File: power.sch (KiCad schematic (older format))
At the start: 28 parts, among them U701 TPS61022, U702 TLV62585

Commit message: Continue part picking
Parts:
- D701: value BAT42 -> BAS16; footprint Diode_SMD:D_SOD-123 -> Diode_SMD:D_SOT-23_ANK; Current (none) -> 150mA; Digikey BAT42W-E3-08CT-ND -> BAS16-FDICT-ND; LCSC (none) -> C69162*; MPN BAT42W-E3-08 -> BAS16-7-F; Note DIODE SCHOTTKY 30V 200MA SOD123 -> DIODE GEN PURP 75V 200MA SOT23-3
- gave numbers to parts that had none: 8
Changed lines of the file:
@@
 P 2950 1000
 F 0 "D701" H 2950 784 50  0000 C CNN
-F 1 "BAT42" H 2950 875 50  0000 C CNN
-F 2 "Diode_SMD:D_SOD-123" H 2950 1000 50  0001 C CNN
+F 1 "BAS16" H 2950 875 50  0000 C CNN
+F 2 "Diode_SMD:D_SOT-23_ANK" H 2950 1000 50  0001 C CNN
 F 3 "~" H 2950 1000 50  0001 C CNN
-F 4 "BAT42W-E3-08" H 2950 1000 50  0001 C CNN "MPN"
-F 5 "BAT42W-E3-08CT-ND" H 2950 1000 50  0001 C CNN "Digikey"
-F 6 "DIODE SCHOTTKY 30V 200MA SOD123" H 2950 1000 50  0001 C CNN "Note"
+F 4 "BAS16-7-F" H 2950 1000 50  0001 C CNN "MPN"
+F 5 "BAS16-FDICT-ND" H 2950 1000 50  0001 C CNN "Digikey"
+F 6 "DIODE GEN PURP 75V 200MA SOT23-3" H 2950 1000 50  0001 C CNN "Note"
+F 7 "150mA" H 2950 1000 50  0001 C CNN "Current"
+F 8 "C69162*" H 2950 1000 50  0001 C CNN "LCSC"
 	1    2950 1000
 	-1   0    0    1
@@
 AR Path="/5FAC6B33/5FBB8CF8" Ref="R?"  Part="1"
 AR Path="/5FCEDB09/5FAC6B33/5FBB8CF8" Ref="R?"  Part="1"
-AR Path="/5FAF778C/5FBB8CF8" Ref="R?"  Part="1"
-F 0 "R?" V 3450 3750 50  0000 C CNN
+AR Path="/5FAF778C/5FBB8CF8" Ref="R804"  Part="1"
+F 0 "R804" V 3450 3750 50  0000 C CNN
 F 1 "59k" V 3350 3750 50  0000 C CNN
 F 2 "Resistor_SMD:R_0603_1608Metric" H 3600 3750 50  0001 C CNN
@@
 $EndComp
 $Comp
-L power:+BATT #PWR?
+L power:+BATT #PWR0198
 U 1 1 5FE17E12
 P 950 1700
-F 0 "#PWR?" H 950 1550 50  0001 C CNN
+F 0 "#PWR0198" H 950 1550 50  0001 C CNN
 F 1 "+BATT" H 965 1873 50  0000 C CNN
 F 2 "" H 950 1700 50  0001 C CNN
@@
 	1250 3650 1600 3650
 $Comp
-L Device:Q_PMOS_GSD Q?
+L Device:Q_PMOS_GSD Q801
 U 1 1 5FAACE37
 P 5550 1950
-AR Path="/5FAF778C/5FAACE37" Ref="Q?"  Part="1"
+AR Path="/5FAF778C/5FAACE37" Ref="Q801"  Part="1"
 AR Path="/5FCEDB09/5FAC6B33/5FAACE37" Ref="Q?"  Part="1"
-F 0 "Q?" V 5892 1950 50  0000 C CNN
+F 0 "Q801" V 5892 1950 50  0000 C CNN
 F 1 "DMMT5401" V 5801 1950 50  0000 C CNN
 F 2 "Package_TO_SOT_SMD:SOT-23-6" H 5750 2050 50  0001 C CNN
@@
 $EndComp
 $Comp
-L Device:Q_DUAL_PNP_PNP_C1B1B2C2E2E1 Q?
+L Device:Q_DUAL_PNP_PNP_C1B1B2C2E2E1 Q802
 U 1 1 5FAACE41
 P 5200 2200
-AR Path="/5FAF778C/5FAACE41" Ref="Q?"  Part="1"
+AR Path="/5FAF778C/5FAACE41" Ref="Q802"  Part="1"
 AR Path="/5FCEDB09/5FAC6B33/5FAACE41" Ref="Q?"  Part="1"
-F 0 "Q?" H 5391 2200 50  0000 L CNN
+F 0 "Q802" H 5391 2200 50  0000 L CNN
 F 1 "DMMT5401" H 5391 2245 50  0001 L CNN
 F 2 "Package_TO_SOT_SMD:SOT-23-6" H 5400 2300 50  0001 C CNN
@@
 P 5100 2650
 AR Path="/5FAACE54" Ref="R?"  Part="1"
-AR Path="/5FAF778C/5FAACE54" Ref="R?"  Part="1"
+AR Path="/5FAF778C/5FAACE54" Ref="R802"  Part="1"
 AR Path="/5FCEDB09/5FAC6B33/5FAACE54" Ref="R?"  Part="1"
-F 0 "R?" H 5168 2696 50  0000 L CNN
+F 0 "R802" H 5168 2696 50  0000 L CNN
 F 1 "10k" H 5168 2605 50  0000 L CNN
 F 2 "Resistor_SMD:R_0603_1608Metric" H 5100 2650 60  0001 C CNN
@@
 P 6000 2650
 AR Path="/5FED2126/5FAACE5A" Ref="R?"  Part="1"
-AR Path="/5FAF778C/5FAACE5A" Ref="R?"  Part="1"
+AR Path="/5FAF778C/5FAACE5A" Ref="R803"  Part="1"
 AR Path="/5FCEDB09/5FAC6B33/5FAACE5A" Ref="R?"  Part="1"
-F 0 "R?" H 5932 2604 50  0000 R CNN
+F 0 "R803" H 5932 2604 50  0000 R CNN
 F 1 "47.5k" H 5932 2695 50  0000 R CNN
 F 2 "Resistor_SMD:R_0603_1608Metric" H 6000 2650 60  0001 C CNN
@@
 	6000 2500 6000 2450
 $Comp
-L power:GND #PWR?
+L power:GND #PWR0199
 U 1 1 5FAACE63
 P 6000 2850
-AR Path="/5FAF778C/5FAACE63" Ref="#PWR?"  Part="1"
+AR Path="/5FAF778C/5FAACE63" Ref="#PWR0199"  Part="1"
 AR Path="/5FCEDB09/5FAC6B33/5FAACE63" Ref="#PWR?"  Part="1"
-F 0 "#PWR?" H 6000 2600 50  0001 C CNN
+F 0 "#PWR0199" H 6000 2600 50  0001 C CNN
 F 1 "GND" H 6005 2677 50  0000 C CNN
 F 2 "" H 6000 2850 50  0001 C CNN
@@
 	6000 2850 6000 2800
 $Comp
-L power:GND #PWR?
+L power:GND #PWR0200
 U 1 1 5FAACE6A
 P 5100 2850
-AR Path="/5FAF778C/5FAACE6A" Ref="#PWR?"  Part="1"
+AR Path="/5FAF778C/5FAACE6A" Ref="#PWR0200"  Part="1"
 AR Path="/5FCEDB09/5FAC6B33/5FAACE6A" Ref="#PWR?"  Part="1"
-F 0 "#PWR?" H 5100 2600 50  0001 C CNN
+F 0 "#PWR0200" H 5100 2600 50  0001 C CNN
 F 1 "GND" H 5105 2677 50  0000 C CNN
 F 2 "" H 5100 2850 50  0001 C CNN
@@
 	5550 2150 5550 2450
 $Comp
-L Device:Q_DUAL_PNP_PNP_C1B1B2C2E2E1 Q?
+L Device:Q_DUAL_PNP_PNP_C1B1B2C2E2E1 Q803
 U 1 1 5FAACE79
 P 5900 2200
-AR Path="/5FAF778C/5FAACE79" Ref="Q?"  Part="1"
+AR Path="/5FAF778C/5FAACE79" Ref="Q803"  Part="1"
 AR Path="/5FCEDB09/5FAC6B33/5FAACE79" Ref="Q?"  Part="2"
-F 0 "Q?" H 6091 2154 50  0000 L CNN
+F 0 "Q803" H 6091 2154 50  0000 L CNN
 F 1 "DMMT5401" H 6091 2245 50  0000 L CNN
 F 2 "Package_TO_SOT_SMD:SOT-23-6" H 6100 2300 50  0001 C CNN
@@
 AR Path="/5E5C8043/5FC95C56" Ref="R?"  Part="1"
 AR Path="/5E715318/5FC95C56" Ref="R?"  Part="1"
-AR Path="/5FAF778C/5FC95C56" Ref="R?"  Part="1"
-F 0 "R?" H 1982 1904 50  0000 R CNN
+AR Path="/5FAF778C/5FC95C56" Ref="R801"  Part="1"
+F 0 "R801" H 1982 1904 50  0000 R CNN
 F 1 "100k" H 1982 1995 50  0000 R CNN
 F 2 "Resistor_SMD:R_0603_1608Metric" V 2090 1940 50  0001 C CNN
@@
 	2550 2050 2600 2050
 $Comp
-L power:+BATT #PWR?
+L power:+BATT #PWR0201
 U 1 1 5FCEFB73
 P 1200 5400
-F 0 "#PWR?" H 1200 5250 50  0001 C CNN
+F 0 "#PWR0201" H 1200 5250 50  0001 C CNN
 F 1 "+BATT" H 1215 5573 50  0000 C CNN
 F 2 "" H 1200 5400 50  0001 C CNN
@@
 $EndComp
 $Comp
-L Connector_Generic:Conn_01x02 J?
+L Connector_Generic:Conn_01x02 J801
 U 1 1 5FCF08CD
 P 1450 5500
-F 0 "J?" H 1530 5492 50  0000 L CNN
+F 0 "J801" H 1530 5492 50  0000 L CNN
 F 1 "Conn_01x02" H 1530 5401 50  0000 L CNN
 F 2 "Connector_PinHeader_2.54mm:PinHeader_1x02_P2.54mm_Vertical" H 1450 5500 50  0001 C CNN
@@
 	1200 5600 1200 5700
 $Comp
-L power:GND #PWR?
+L power:GND #PWR0202
 U 1 1 5FCF766A
 P 1200 5700
-AR Path="/5FAF778C/5FCF766A" Ref="#PWR?"  Part="1"
+AR Path="/5FAF778C/5FCF766A" Ref="#PWR0202"  Part="1"
 AR Path="/5FCEDB09/5FAC6B33/5FCF766A" Ref="#PWR?"  Part="1"
-F 0 "#PWR?" H 1200 5450 50  0001 C CNN
+F 0 "#PWR0202" H 1200 5450 50  0001 C CNN
 F 1 "GND" H 1205 5527 50  0000 C CNN
 F 2 "" H 1200 5700 50  0001 C CNN

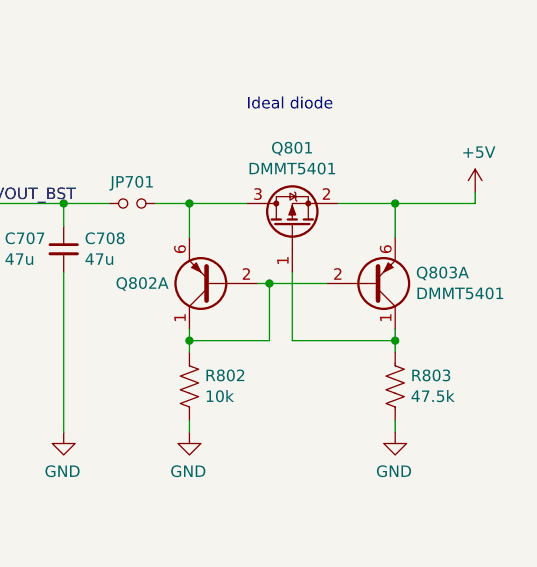
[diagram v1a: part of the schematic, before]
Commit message: Modified layout for Smoke, Fixed Ideal Diode
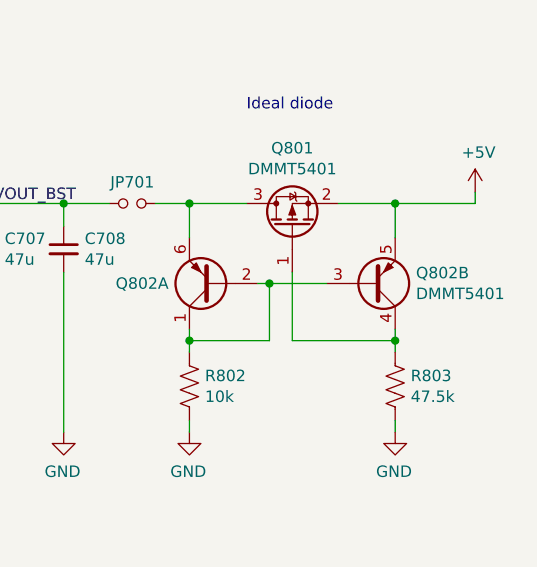
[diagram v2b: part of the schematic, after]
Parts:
- renumbered Q803 to Q802
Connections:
- net +5V: now also Q802.5 (E2); no longer Q802.6 (E1)
- net at Q801.1 (G), R803.2: now also Q802.4 (C2); no longer Q802.1 (C1)
- net at Q802.1 (C1), Q802.2 (B1), R802.1: now also Q802.3 (B2); no longer Q802.2 (B1)
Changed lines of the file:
@@
 	5550 2150 5550 2450
 $Comp
-L Device:Q_DUAL_PNP_PNP_C1B1B2C2E2E1 Q803
-U 1 1 5FAACE79
+L Device:Q_DUAL_PNP_PNP_C1B1B2C2E2E1 Q802
+U 2 1 5FAACE79
 P 5900 2200
-AR Path="/5FAF778C/5FAACE79" Ref="Q803"  Part="1"
+AR Path="/5FAF778C/5FAACE79" Ref="Q802"  Part="2"
 AR Path="/5FCEDB09/5FAC6B33/5FAACE79" Ref="Q?"  Part="2"
-F 0 "Q803" H 6091 2154 50  0000 L CNN
+F 0 "Q802" H 6091 2154 50  0000 L CNN
 F 1 "DMMT5401" H 6091 2245 50  0000 L CNN
 F 2 "Package_TO_SOT_SMD:SOT-23-6" H 6100 2300 50  0001 C CNN
@@
 F 6 "TRANS 2PNP 150V 0.2A SOT26" H 5900 2200 50  0001 C CNN "Note"
 F 7 "C154733" H 5900 2200 50  0001 C CNN "LCSC"
-	1    5900 2200
+	2    5900 2200
 	1    0    0    1
 $EndComp

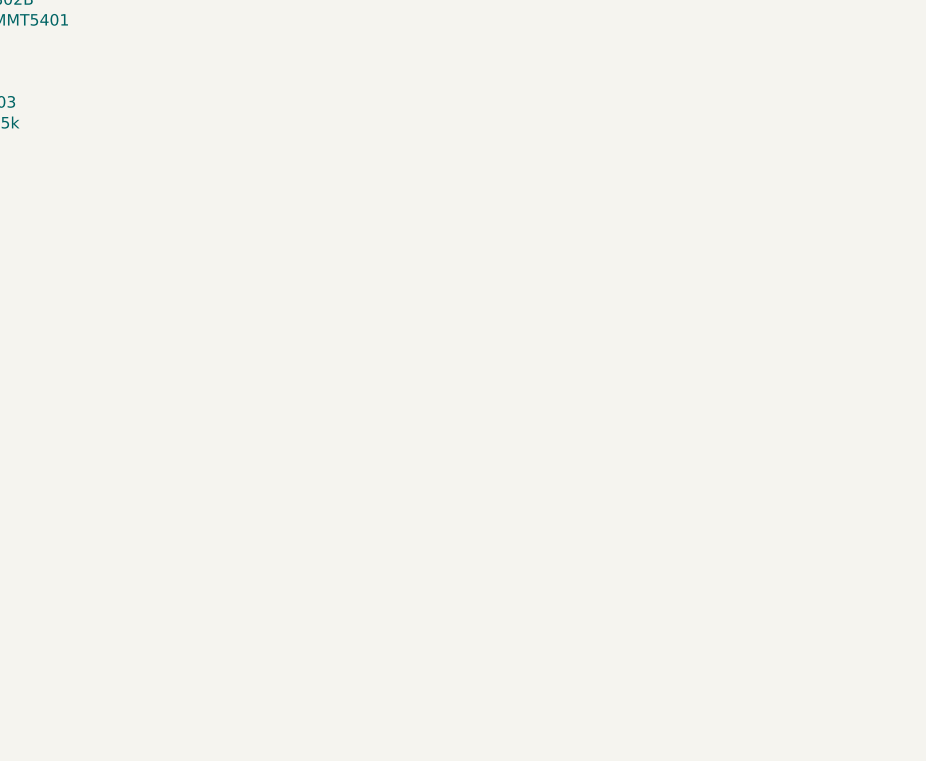
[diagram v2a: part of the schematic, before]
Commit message: Added battery charger schematic
Annotated
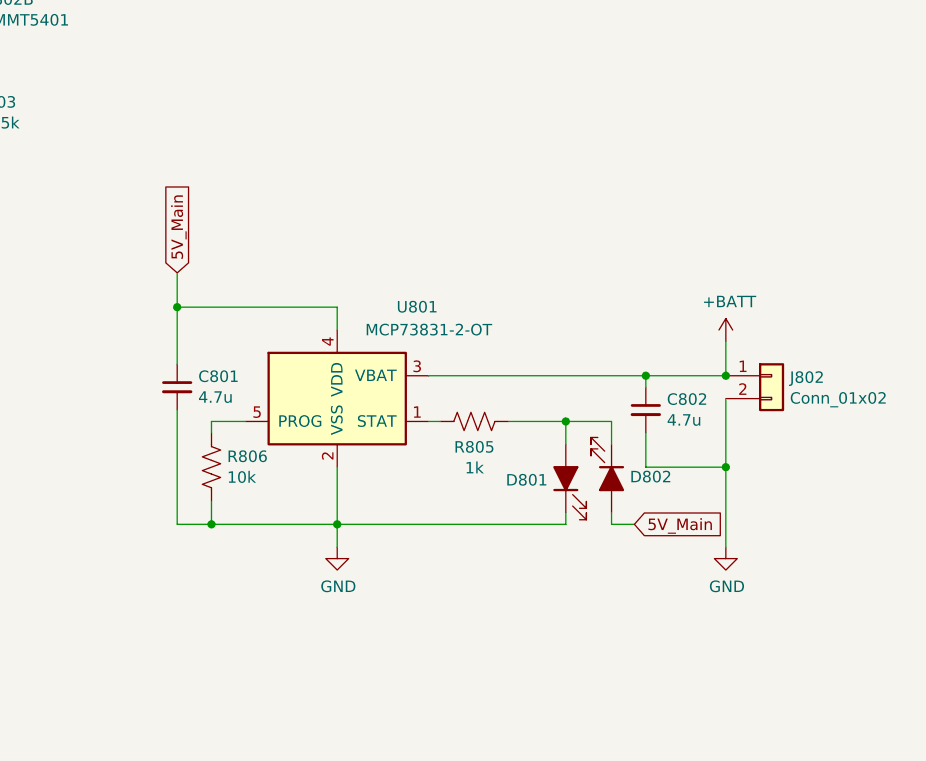
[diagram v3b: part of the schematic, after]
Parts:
- added C801, C802: 4.7u, Capacitor_SMD:C_0603_1608Metric, symbol Device:C_Small
- added D801, D802: LED_ALT, LED_SMD:LED_0603_1608Metric, symbol Device:LED_ALT
- added J802: Conn_01x02, Connector_JST:JST_PH_B2B-PH-K_1x02_P2.00mm_Vertical, symbol Connector_Generic:Conn_01x02
- added R805: 1k, Resistor_SMD:R_0603_1608Metric, symbol Device:R_US
- added R806: 10k, Resistor_SMD:R_0603_1608Metric, symbol Device:R_US
- added U801: MCP73831-2-OT, Package_TO_SOT_SMD:SOT-23-5, symbol Battery_Management:MCP73831-2-OT
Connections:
- net +BATT: now also C802.1, J802.1 (Pin_1), U801.3 (VBAT)
- net GND: now also C801.2, C802.2, D801.1 (K), J802.2 (Pin_2), R806.2, U801.2 (VSS)
- new net: R805.1, U801.1 (STAT)
- new net: R806.1, U801.5 (PROG)
- new net: D801.2 (A), D802.1 (K), R805.2
- new net 5V_Main: C801.1, D802.2 (A), U801.4 (VDD)

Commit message: Cleaned up, Annotated
Added Global 5V_Main net, solder jumper for battery charger, jumper for speaker and speaker_alt, added parts for battery charger
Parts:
- added JP801: Jumper_NO_Small, Jumper:SolderJumper-2_P1.3mm_Open_TrianglePad1.0x1.5mm, symbol Device:Jumper_NO_Small
- J802: Digikey (none) -> B2B-PH-K-S(LF)(SN); LCSC (none) -> C131337; MPN (none) -> B2B-PH-K-S(LF)(SN); Note (none) -> CONN HEADER VERT 2POS 2MM
- U801: Digikey (none) -> MCP73831T-2ACI/OTCT-ND; LCSC (none) -> C424093; MPN (none) -> MCP73831T-2ACI/OT; Note (none) -> IC CONTROLLR LI-ION 4.2V SOT23-5
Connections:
- net 5V_Main: now also JP801.2; no longer C801.1, U801.4 (VDD)
- new net: C801.1, JP801.1, U801.4 (VDD)
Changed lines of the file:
@@
 F 2 "Connector_JST:JST_PH_B2B-PH-K_1x02_P2.00mm_Vertical" H 9550 3800 50  0001 C CNN
 F 3 "~" H 9550 3800 50  0001 C CNN
+F 4 "B2B-PH-K-S(LF)(SN)" H 9550 3800 50  0001 C CNN "Digikey"
+F 5 "C131337" H 9550 3800 50  0001 C CNN "LCSC"
+F 6 "B2B-PH-K-S(LF)(SN)" H 9550 3800 50  0001 C CNN "MPN"
+F 7 "CONN HEADER VERT 2POS 2MM" H 9550 3800 50  0001 C CNN "Note"
 	1    9550 3800
 	1    0    0    -1
@@
 	0    1    1    0
 $EndComp
-Connection ~ 6950 3500
 Wire Wire Line
 	7650 3500 7650 3600
@@
 Wire Wire Line
 	6950 4450 7100 4450
-Wire Wire Line
-	6950 3350 6950 3500
 $Comp
 L Device:C_Small C?
@@
 	1    0    0    -1
 $EndComp
-Text GLabel 6950 3350 1    50   Input ~ 0
+Text GLabel 6950 3050 1    50   Input ~ 0
 5V_Main
 $Comp
@@
 F 2 "Package_TO_SOT_SMD:SOT-23-5" H 7700 3650 50  0001 L CIN
 F 3 "http://ww1.microchip.com/downloads/en/DeviceDoc/20001984g.pdf" H 7500 3850 50  0001 C CNN
+F 4 "MCP73831T-2ACI/OTCT-ND" H 7650 3900 50  0001 C CNN "Digikey"
+F 5 "C424093" H 7650 3900 50  0001 C CNN "LCSC"
+F 6 "MCP73831T-2ACI/OT" H 7650 3900 50  0001 C CNN "MPN"
+F 7 "IC CONTROLLR LI-ION 4.2V SOT23-5" H 7650 3900 50  0001 C CNN "Note"
 	1    7650 3900
 	1    0    0    -1
@@
 Wire Wire Line
 	8650 4000 8850 4000
+$Comp
+L Device:Jumper_NO_Small JP801
+U 1 1 5FE9A978
+P 6950 3350
+AR Path="/5FAF778C/5FE9A978" Ref="JP801"  Part="1"
+AR Path="/5FCEDB09/5FAC6B33/5FE9A978" Ref="JP?"  Part="1"
+F 0 "JP801" H 6950 3443 50  0000 C CNN
+F 1 "Jumper_NO_Small" H 6950 3444 50  0001 C CNN
+F 2 "Jumper:SolderJumper-2_P1.3mm_Open_TrianglePad1.0x1.5mm" H 6950 3350 50  0001 C CNN
+F 3 "~" H 6950 3350 50  0001 C CNN
+F 4 "1" H 6950 3350 50  0001 C CNN "DNP"
+	1    6950 3350
+	0    -1   -1   0
+$EndComp
+Wire Wire Line
+	6950 3050 6950 3250
+Wire Wire Line
+	6950 3450 6950 3500
+Connection ~ 6950 3500
 $EndSCHEMATC

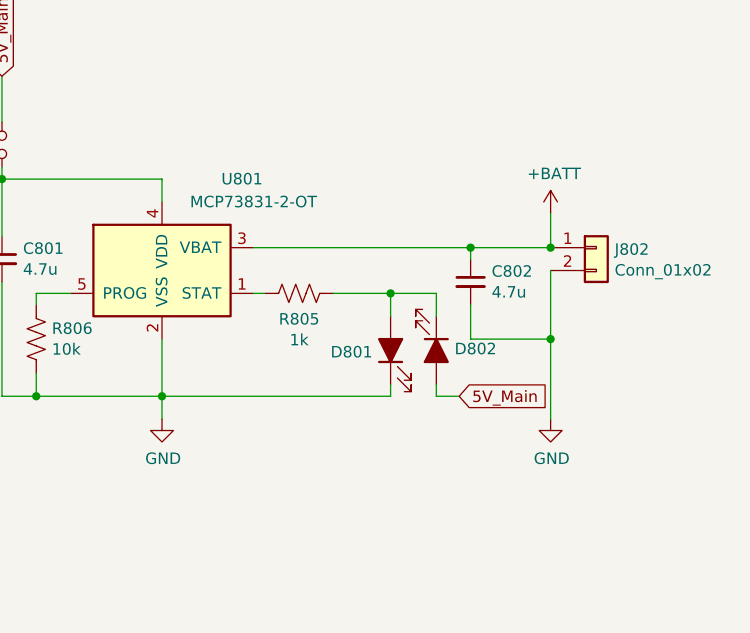
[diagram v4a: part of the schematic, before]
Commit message: Add resistor to battery indicator, battery layout, update font sizes
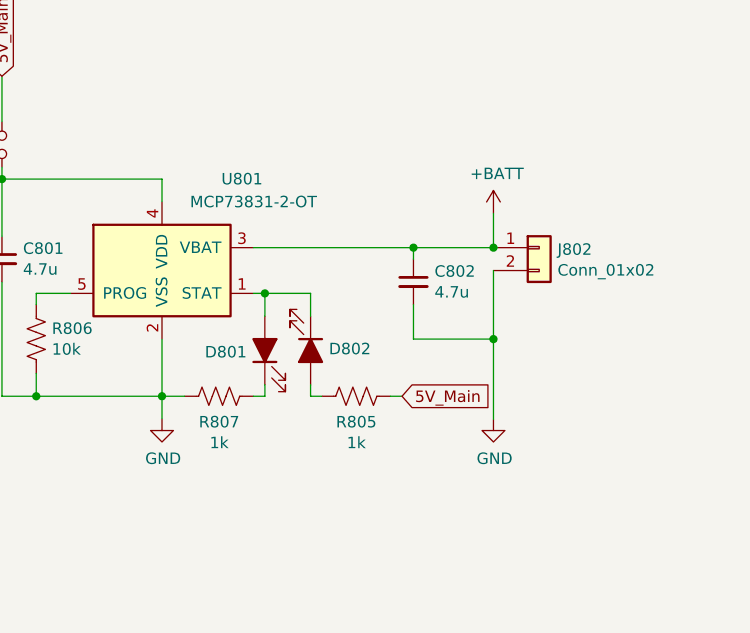
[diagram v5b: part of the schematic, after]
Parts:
- added R807: 1k, Resistor_SMD:R_0603_1608Metric, symbol Device:R_US
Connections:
- net 5V_Main: now also R805.2; no longer D802.2 (A)
- net GND: now also R807.1; no longer D801.1 (K)
- net at U801.1 (STAT): now also D801.2 (A), D802.1 (K); no longer R805.1
- new net: D801.1 (K), R807.2
- new net: D802.2 (A), R805.1
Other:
- moved on the sheet: C802, D801, D802, J802, R805

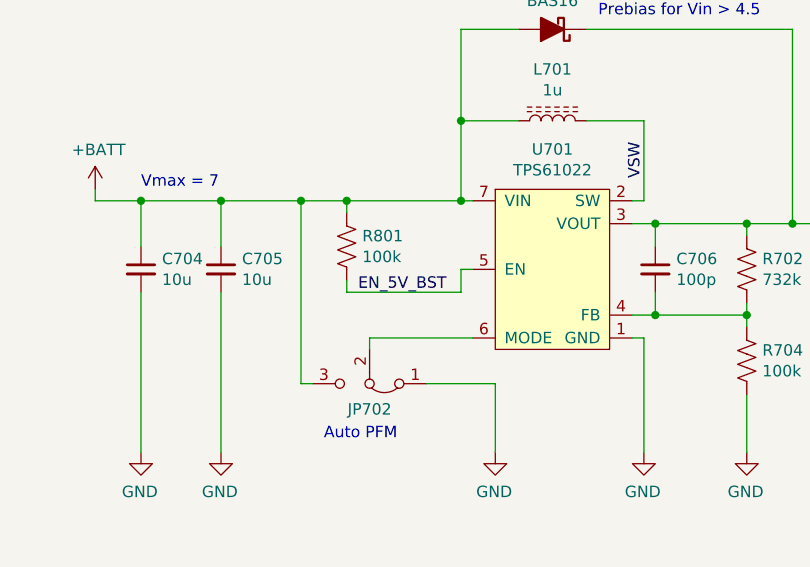
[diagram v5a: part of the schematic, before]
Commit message: 4layer layout WIP, 90%.
Changed SCD30 to reverse mount. 
Connected RGB led and button to io expander.
Connected all nets to micro.
Add jumper for CTS line.
Nettie GNDA and GND for W5500 Eth.
Changed EN_5V_BST to Global.
Bugfixes net names: LCD_CS
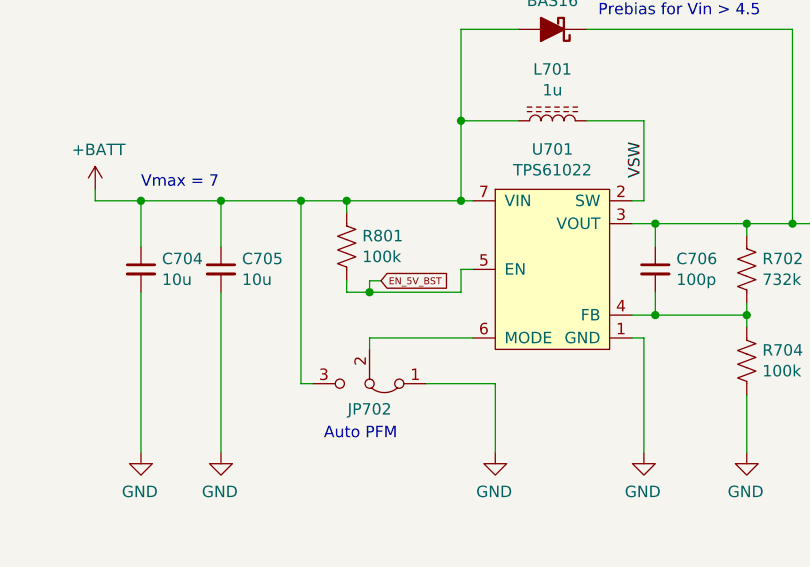
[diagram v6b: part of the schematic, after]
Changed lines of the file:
@@
 Wire Wire Line
 	1850 1750 1850 2550
-Text Label 2100 2150 0    50   ~ 0
-EN_5V_BST
 Wire Wire Line
 	1250 3650 1600 3650
@@
 	2050 2100 2050 2150
 Wire Wire Line
-	2050 2150 2550 2150
+	2050 2150 2150 2150
 Wire Wire Line
 	2550 2150 2550 2050
@@
 Wire Wire Line
 	8050 4000 8100 4000
+Text GLabel 2200 2100 2    30   Input ~ 0
+EN_5V_BST
+Wire Wire Line
+	2200 2100 2150 2100
+Wire Wire Line
+	2150 2100 2150 2150
+Connection ~ 2150 2150
+Wire Wire Line
+	2150 2150 2550 2150
 $EndSCHEMATC
